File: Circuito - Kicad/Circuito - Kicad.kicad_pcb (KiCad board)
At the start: 2 copper layers, 12 parts, among them U1 4N25, U2 MOC3021M

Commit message: PCB Improvement
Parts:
- added ?: , , F.Cu at (146.4, 126.0)
- added ?: , , F.Cu at (194.6, 127.4)
- added ?: , , F.Cu at (189.6, 75.3)
- added ?: , , F.Cu at (161.6, 75.3)
- Triac1: footprint BT136:TO220AB -> BT139-600E:TO255P1040X460X1975-3
- moved Triac1 6.53 mm to (118.5, 78.6)

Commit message: Kicad Improvement
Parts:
- removed Sensor1: TB_1X3, EESTN5:BORNERA3
- added Potenciometro1: TB_1X3, EESTN5:BORNERA3, F.Cu at (133.5, 136.2)
- moved G*** 11.4 mm to (187.2, 59.8)
- moved R4 0.99 mm to (121.2, 106.1)
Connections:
- SH1 pad 5V: unconnected-(SH1-Pad5V) -> VCC
- SH1 pad GND1: unconnected-(SH1-GND/1-PadGND1) -> GND
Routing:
- net VCC: track 31.7 -> 166.2 mm
- net PIN_A0: track 120.1 -> 108.4 mm
- net Net-(R4-Pad1): track 69.6 -> 67.0 mm
- net Vivo: track 109.9 -> 108.5 mm
- net Net-(R1-Pad2): track 119.2 -> 120.4 mm

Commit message: Kicad | Schematic Improvement
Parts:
- removed ? (x4): , 
- removed Potenciometro1: TB_1X3, EESTN5:BORNERA3
- removed SH1: ARDUINO_as_UNO, EESTN5:ARDUINO_UNO_R2_CONTOUR
- added Alimentación1: Alimentación | Arduino, EESTN5:Pin_Header_2, F.Cu at (192.6, 102.4)
- added Datos1: Datos, EESTN5:Pin_Header_3, F.Cu at (186.8, 84.8)
- Alterna1: value TB_1X2 -> Alterna
- Calentador1: value TB_1X2 -> Calentador
- Triac1: value Generic_Triac_A1A2G -> Triac
- moved R1 118.1 mm to (200.0, 66.9), turned to 0 degrees
- moved R3 97.0 mm to (200.0, 75.0), turned to 0 degrees
- moved R4 83.3 mm to (200.0, 79.0), turned to 0 degrees
- moved R2 47.1 mm to (200.0, 70.9), turned to 0 degrees
- moved U2 45.6 mm to (110.1, 101.9), turned to 90 degrees
- moved G*** 40.1 mm to (225.2, 72.9)
- moved U1 27.8 mm to (165.3, 99.2), turned to 0 degrees
- moved Triac1 27.2 mm to (144.6, 86.3)
- moved Alterna1 21.5 mm to (110.1, 119.1)
- moved Calentador1 19.4 mm to (126.1, 119.1)
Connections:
- R4 pad 1: Net-(R4-Pad1) -> PIN_2
- U1 pad 4: Net-(R4-Pad1) -> PIN_2
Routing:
- net VCC: track 166.2 -> 0.00 mm
- net Net-(R1-Pad2): track 120.4 -> 0.00 mm
- net Vivo: track 108.5 -> 0.00 mm
- net PIN_A0: track 108.4 -> 0.00 mm
- net Net-(Triac1-A2): track 102.9 -> 0.00 mm
- net Net-(R4-Pad1): track 67.0 -> 0.00 mm
- net Net-(R3-Pad2): track 46.0 -> 0.00 mm
- net PIN_7: track 29.0 -> 0.00 mm
- net Neutro: track 25.0 -> 0.00 mm
- net Net-(Triac1-G): track 24.2 -> 0.00 mm
- net Net-(R2-Pad1): track 17.2 -> 0.00 mm
- removed copper zone on B.Cu, net GND

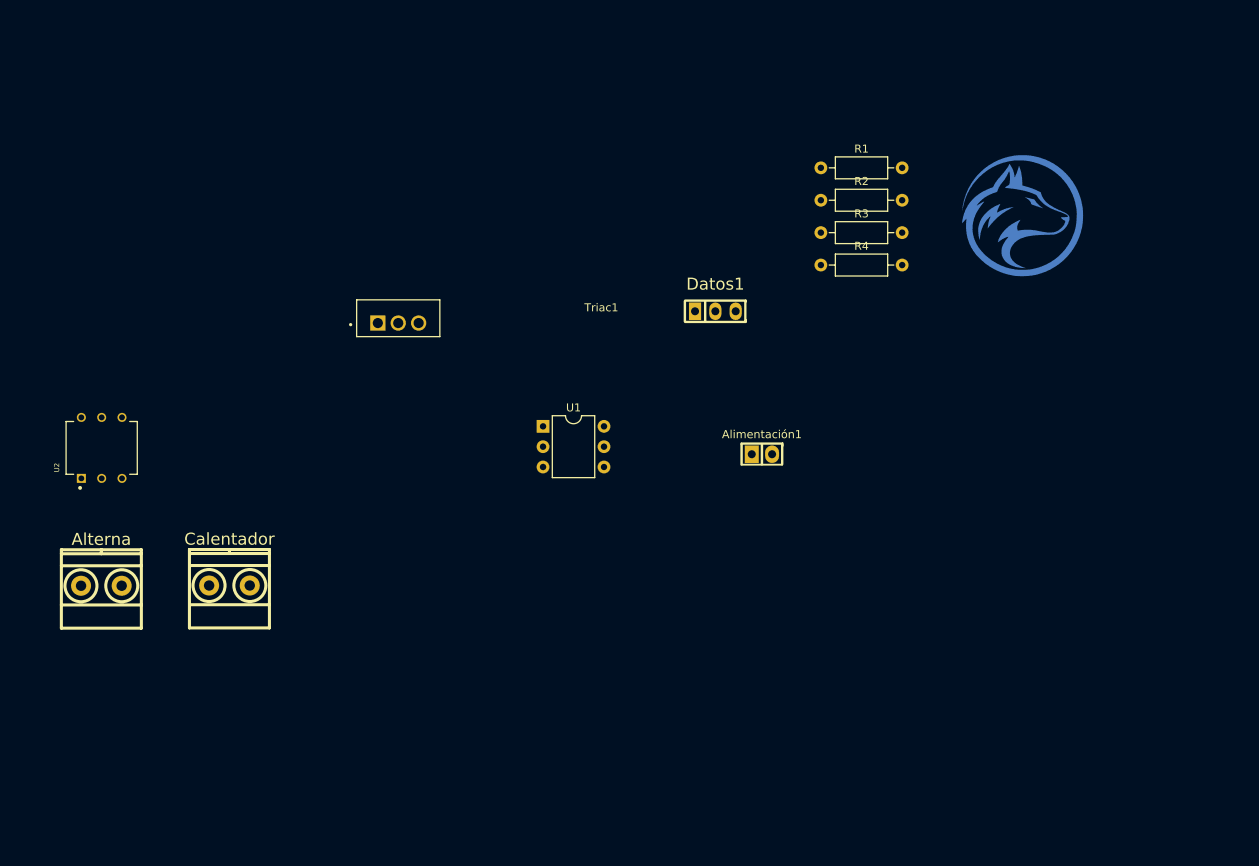
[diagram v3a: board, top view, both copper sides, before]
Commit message: Kicad | PCB Improvement | 6x3,5
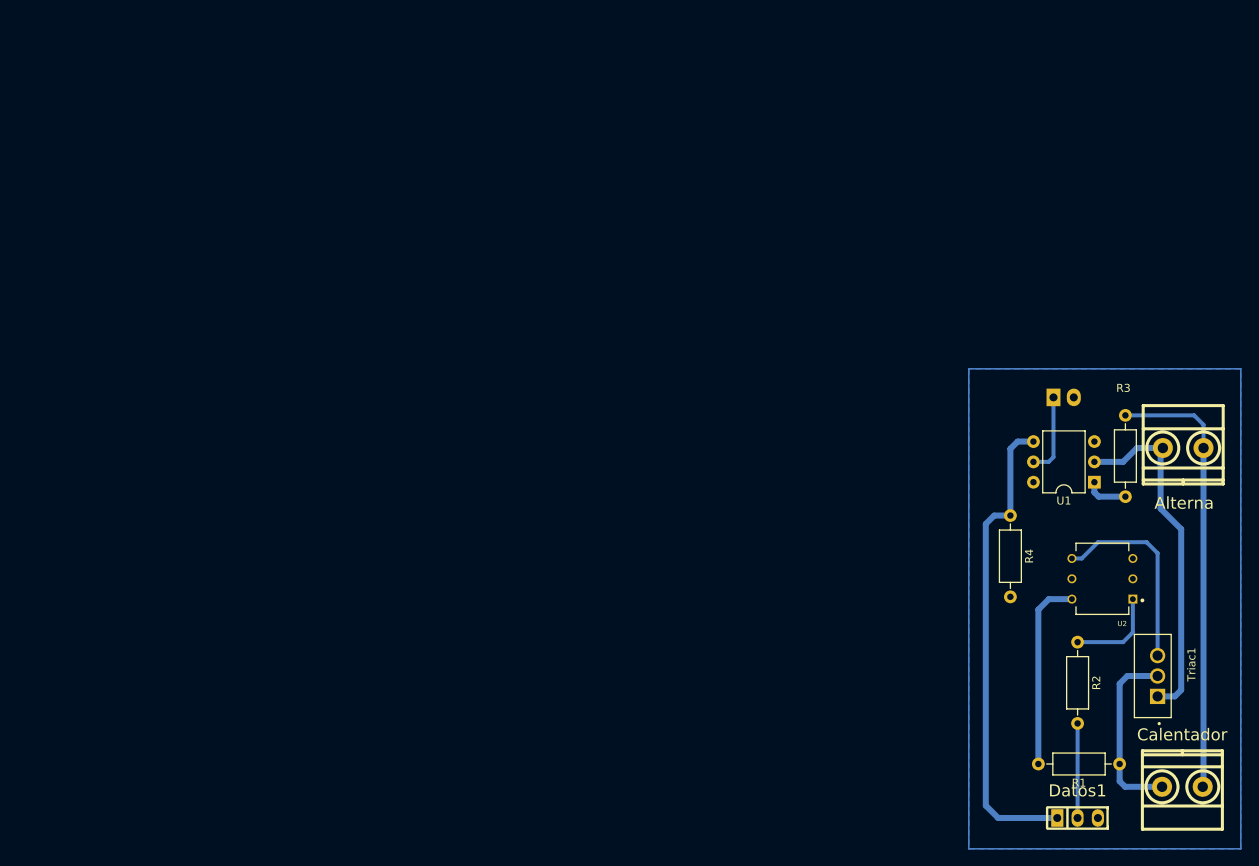
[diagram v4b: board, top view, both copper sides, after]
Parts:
- removed G***: LOGO, Wolfsrudel_Logo:wolfsrudel_logo
- Alimentación1: moved to B.Cu
- moved Alterna1 136.3 mm to (245.3, 101.9), turned to 0 degrees
- moved U2 126.2 mm to (235.2, 118.2), turned to 180 degrees
- moved Calentador1 121.7 mm to (245.2, 144.2)
- moved Triac1 108.1 mm to (242.1, 132.9), turned to 90 degrees
- moved R1 83.4 mm to (237.4, 141.4), turned to 180 degrees
- moved Datos1 77.9 mm to (232.1, 148.2)
- moved U1 69.3 mm to (234.2, 106.2), turned to 180 degrees
- moved R2 63.9 mm to (232.1, 126.2), turned to -90 degrees
- moved R3 44.4 mm to (238.1, 97.8), turned to -90 degrees
- moved R4 39.3 mm to (223.7, 110.3), turned to -90 degrees
- moved Alimentación1 38.3 mm to (230.4, 95.9)
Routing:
- net PIN_2: track 0.00 -> 59.9 mm
- net Neutro: track 0.00 -> 55.6 mm
- net Vivo: track 0.00 -> 44.0 mm
- net Net-(Triac1-G): track 0.00 -> 24.9 mm
- net Net-(R1-Pad2): track 0.00 -> 24.0 mm
- net Net-(Triac1-A2): track 0.00 -> 22.9 mm
- net PIN_7: track 0.00 -> 11.8 mm
- net Net-(R2-Pad1): track 0.00 -> 11.6 mm
- net VCC: track 0.00 -> 10.2 mm
- net Net-(R3-Pad2): track 0.00 -> 5.46 mm
- added copper zone on B.Cu, net GND

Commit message: Kicad | PDF
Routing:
- net Net-(Triac1-G): track 24.9 -> 27.7 mm
